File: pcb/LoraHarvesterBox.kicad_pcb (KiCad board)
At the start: 4 copper layers, 48 x 45.5 mm, 42 parts, among them J1 Conn_01x02_Pin, J2 Conn_01x02_Pin, J3 Conn_01x02_Pin, J4 Conn_01x04_Socket, J5 Conn_01x04_Socket, J6 Conn_01x04_Socket, J7 Conn_01x04_Socket, J8 Conn_01x06_Socket, SW1 SSSS811101, SW2 TS-1088-AR02016, U1 BQ25570, U2 RAK3172-8-SM-I, U3 FM24V10-GTR_C466851

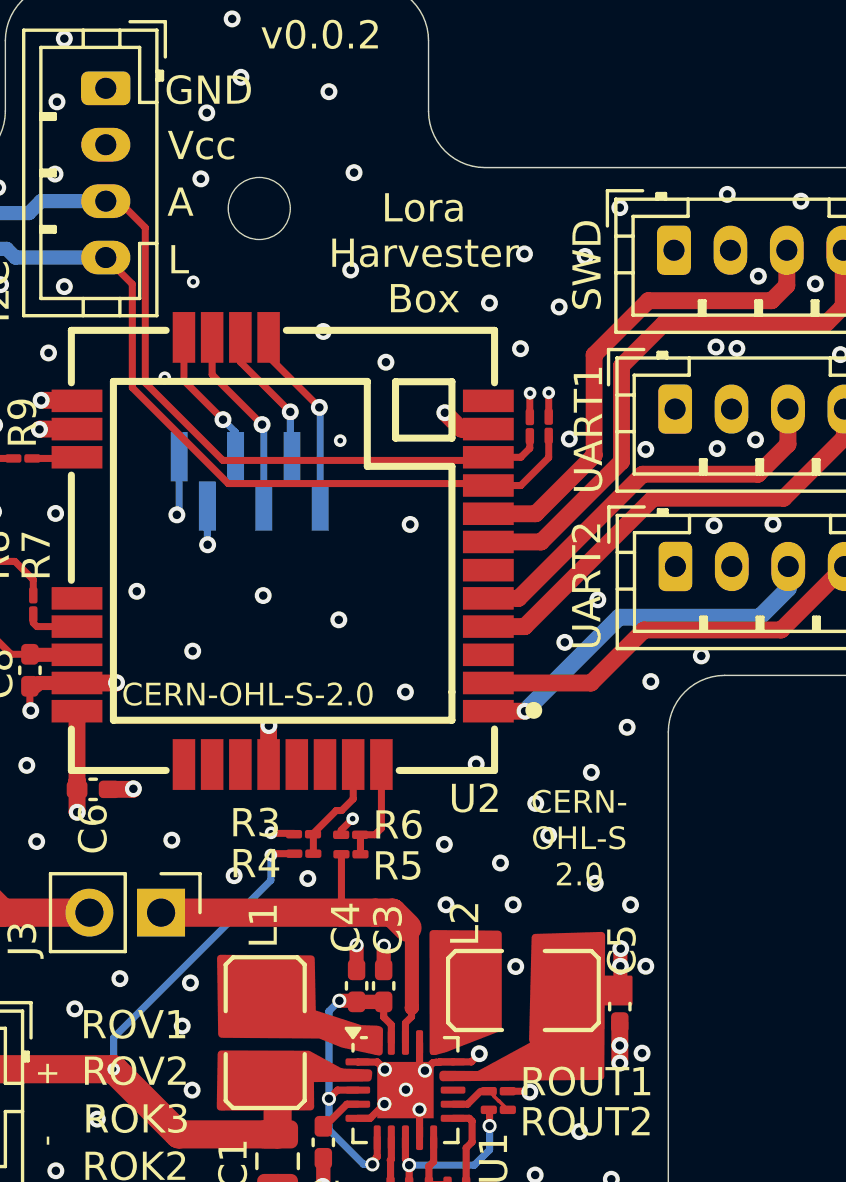
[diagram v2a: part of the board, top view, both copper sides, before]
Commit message: pcb, sch: add resistor values and pretty up the pcb a bit
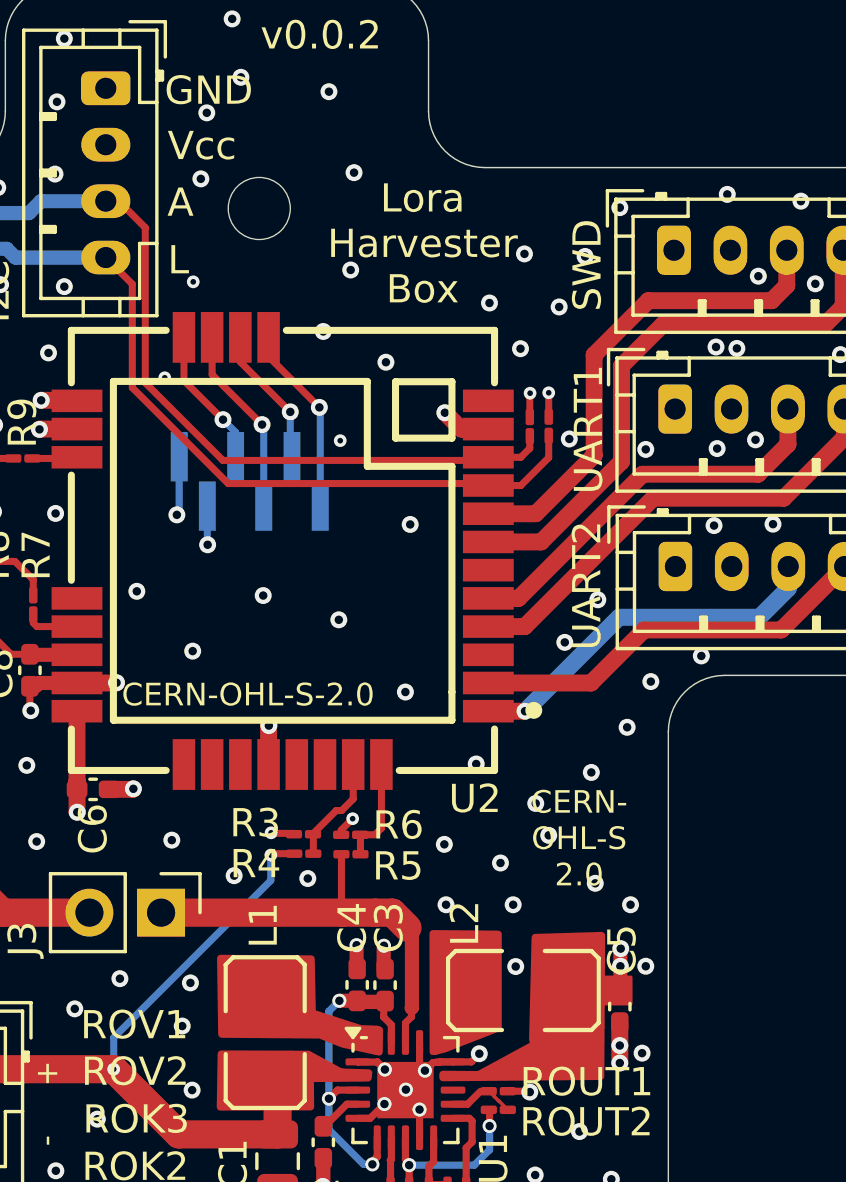
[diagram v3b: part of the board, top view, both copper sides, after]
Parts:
- C1: value C -> 4.7uF
- C2: value C -> 10nF
- C3: renamed from C4; value C -> 0.01uF
- C4: renamed from C3; value CSTOR -> 4.7uF
- ROK1: value R -> 4.3M
- ROK2: value R -> 6.8M
- ROK3: value R -> 1.9M
- ROUT1, ROV2: value R -> 5.1M
- ROUT2: value R -> 7.5M
- ROV1: value R -> 3.9M
- moved C3 1.01 mm to (129.0, 90.0)
- moved C4 0.94 mm to (128.0, 90.0)
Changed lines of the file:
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@@
 			)
 		)
-		(property "Value" "R"
+		(property "Value" "4.3M"
 			(at 0 1 90)
 			(layer "F.Fab")
@@
 	(footprint "Capacitor_SMD:C_0402_1005Metric_Pad0.74x0.62mm_HandSolder"
 		(layer "F.Cu")
-		(at 128.91 90.00625 90)
+		(at 127.97 89.97 90)
 		(descr "Capacitor SMD 0402 (1005 Metric), square (rectangular) end terminal, IPC-7351 nominal with elongated pad for handsoldering. (Body size source: IPC-SM-782 page 76, https://www.pcb-3d.com/wordpress/wp-content/uploads/ipc-sm-782a_amendment_1_and_2.pdf), generated with kicad-footprint-generator")
 		(tags "capacitor handsolder")
-		(property "Reference" "C3"
-			(at 1.98625 0.17 90)
+		(property "Reference" "C4"
+			(at 2.03 -0.16 90)
 			(layer "F.SilkS")
 			(effects
@@
 			)
 		)
-		(property "Value" "CSTOR"
+		(property "Value" "4.7uF"
 			(at 0 1.16 90)
 			(layer "F.Fab")
@@
 			)
 		)
-		(property "Value" "C"
+		(property "Value" "10nF"
 			(at -2.44 5.72 90)
 			(layer "F.Fab")
@@
 			)
 		)
-		(property "Value" "R"
+		(property "Value" "6.8M"
 			(at 0 1 90)
 			(layer "F.Fab")
@@
 			)
 		)
-		(property "Value" "R"
+		(property "Value" "3.9M"
 			(at 0 1 90)
 			(layer "F.Fab")
@@
 	(footprint "Capacitor_SMD:C_0402_1005Metric_Pad0.74x0.62mm_HandSolder"
 		(layer "F.Cu")
-		(at 127.95 90.00375 90)
+		(at 128.96 89.9775 90)
 		(descr "Capacitor SMD 0402 (1005 Metric), square (rectangular) end terminal, IPC-7351 nominal with elongated pad for handsoldering. (Body size source: IPC-SM-782 page 76, https://www.pcb-3d.com/wordpress/wp-content/uploads/ipc-sm-782a_amendment_1_and_2.pdf), generated with kicad-footprint-generator")
 		(tags "capacitor handsolder")
-		(property "Reference" "C4"
-			(at 2.07375 -0.37 90)
+		(property "Reference" "C3"
+			(at 2.0375 0.15 90)
 			(layer "F.SilkS")
 			(effects
@@
 			)
 		)
-		(property "Value" "C"
+		(property "Value" "0.01uF"
 			(at 2.9775 1.51 90)
 			(layer "F.Fab")
@@
 			)
 		)
-		(property "Value" "R"
+		(property "Value" "5.1M"
 			(at 0.2 2.86 0)
 			(layer "F.Fab")
@@
 			)
 		)
-		(property "Value" "C"
+		(property "Value" "4.7uF"
 			(at 0 1.68 270)
 			(layer "F.Fab")
@@
 			)
 		)
-		(property "Value" "R"
+		(property "Value" "1.9M"
 			(at 0.9 5.15 90)
 			(layer "F.Fab")
@@
 			)
 		)
-		(property "Value" "R"
+		(property "Value" "5.1M"
 			(at 0 1 90)
 			(layer "F.Fab")
@@
 			)
 		)
-		(property "Value" "R"
+		(property "Value" "7.5M"
 			(at -9.02 -0.65 0)
 			(layer "F.Fab")
@@
 	)
 	(gr_text "Lora\nHarvester\nBox"
-		(at 130.33 66.25 0)
+		(at 130.29 65.9 0)
 		(layer "F.SilkS")
 		(effects

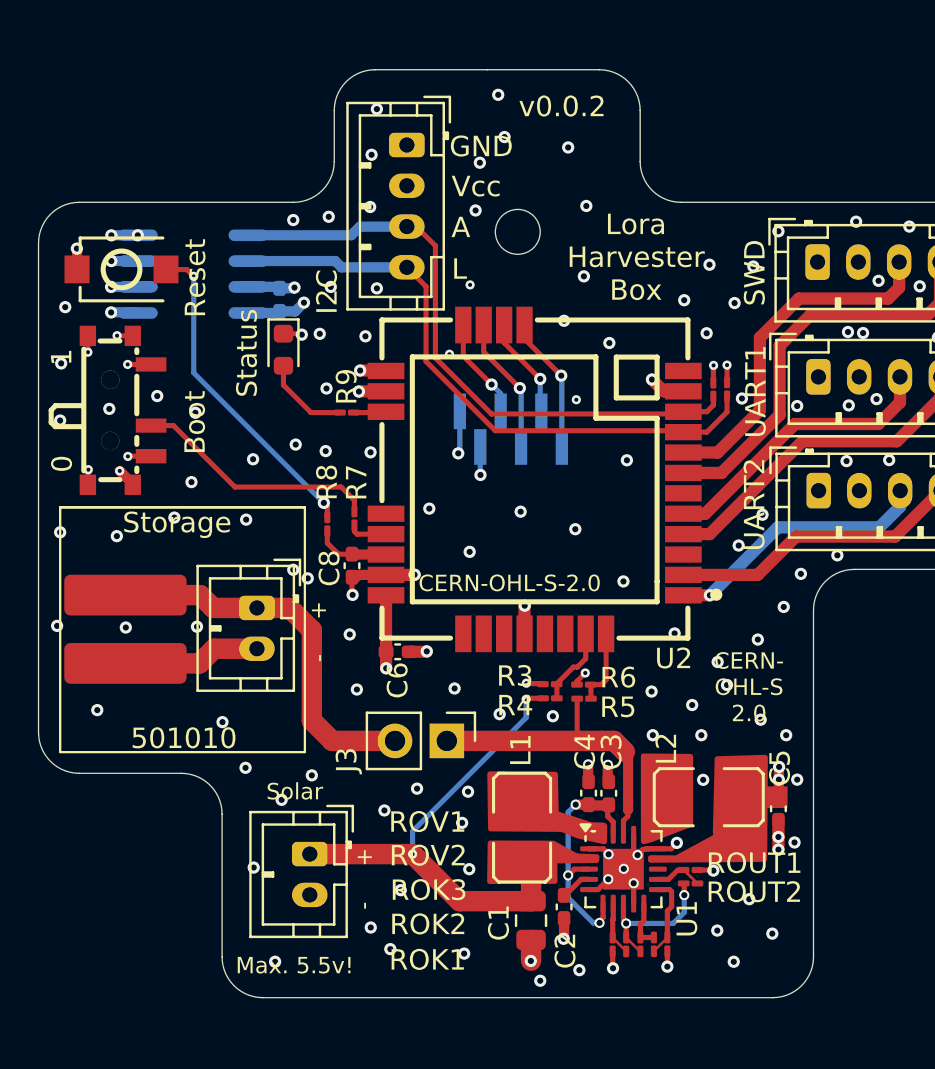
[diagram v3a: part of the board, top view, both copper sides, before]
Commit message: pcb, sch: connect VBAT_OK signal to mirocontroller
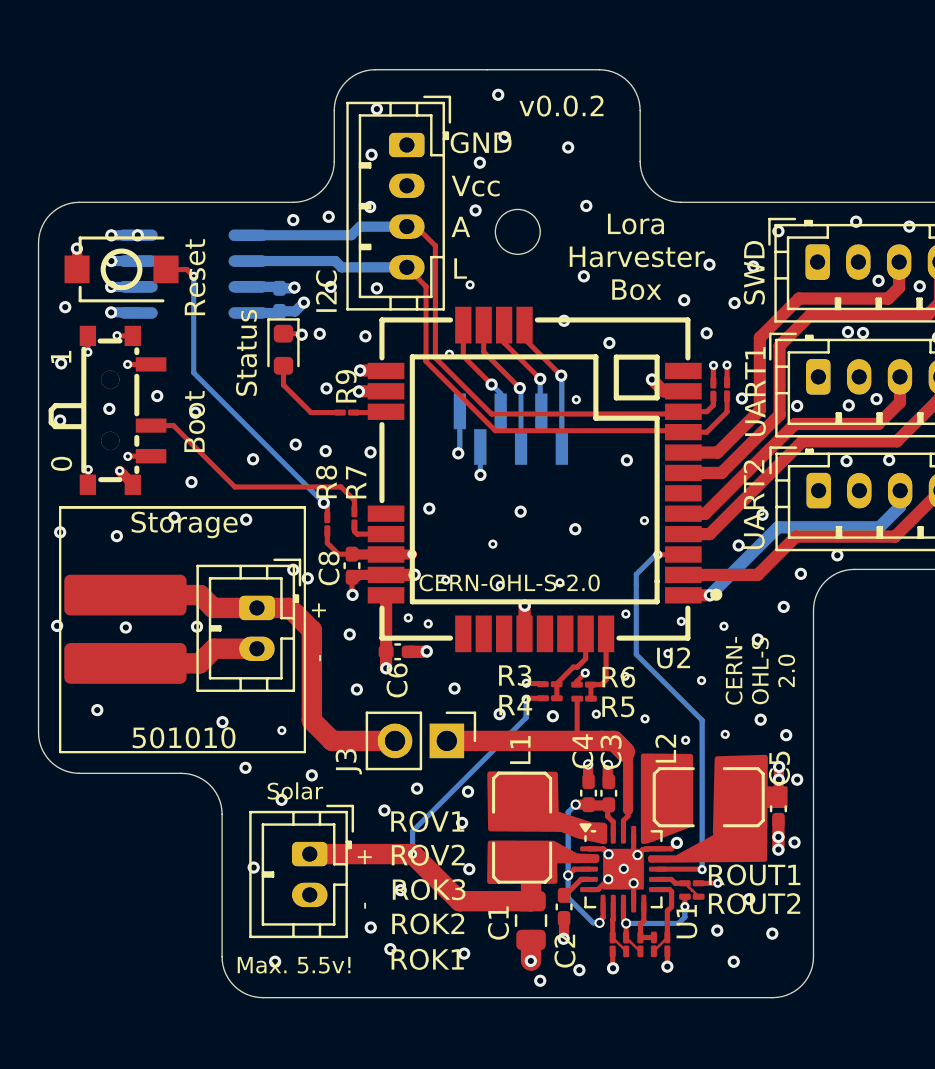
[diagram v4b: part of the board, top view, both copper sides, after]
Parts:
- moved ROUT1 0.65 mm to (133.0, 94.4)
- moved ROUT2 0.65 mm to (133.0, 95.0)
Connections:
- U1 pad 13: unconnected-(U1-VBAT_OK-Pad13) -> /VBAT_OK
- U2 pad 3: unconnected-(U2-PA15/PIN_A4-Pad3) -> /VBAT_OK
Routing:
- net /VBAT_OK: track 0.00 -> 20.7 mm, vias 0 -> 2
- net /RST: track 3.49 -> 4.76 mm, vias 0 -> 1
- net GND: track 51.5 -> 51.6 mm, vias 157 -> 165

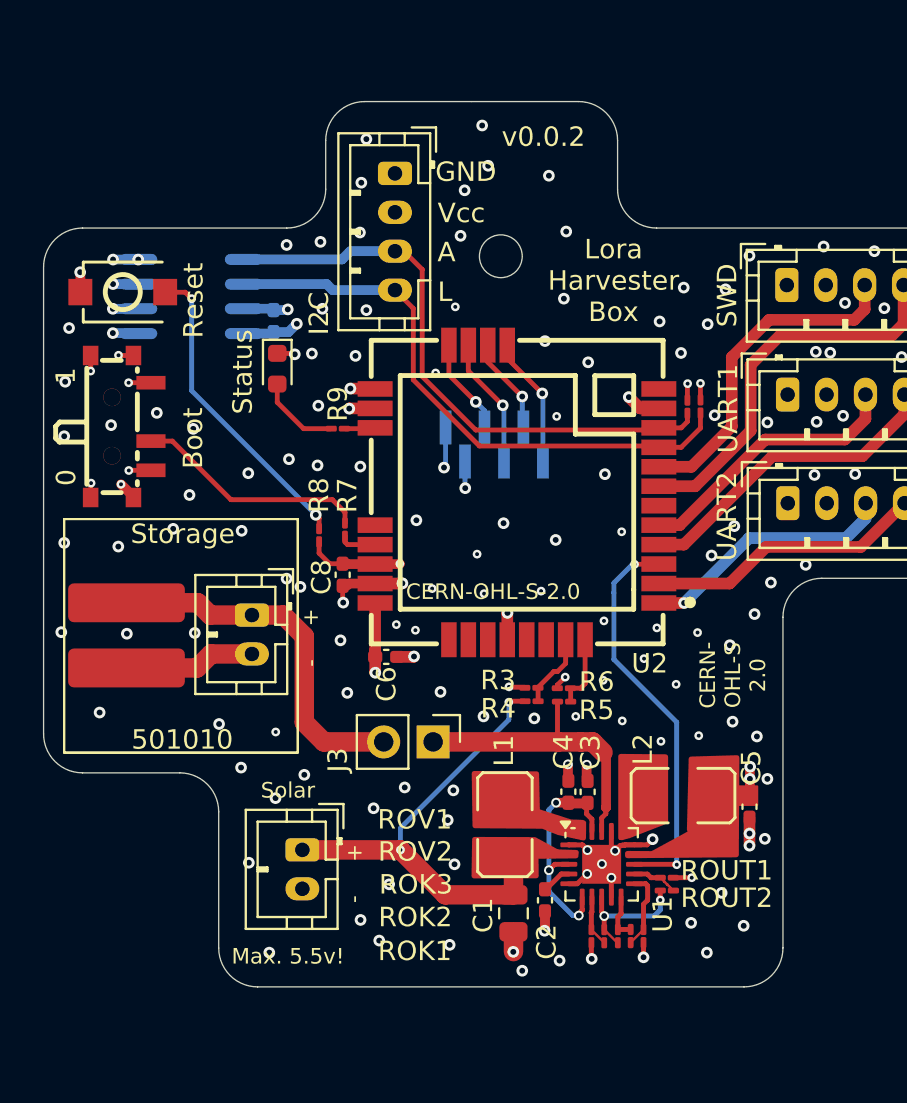
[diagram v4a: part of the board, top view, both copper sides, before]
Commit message: pcb, sch, doc: replace all 402 components with 0603 or 0805.
I cannot solder 0402 in my homelab :-( It starts with the mis-aligned tweezers
and ends with shaking hands.
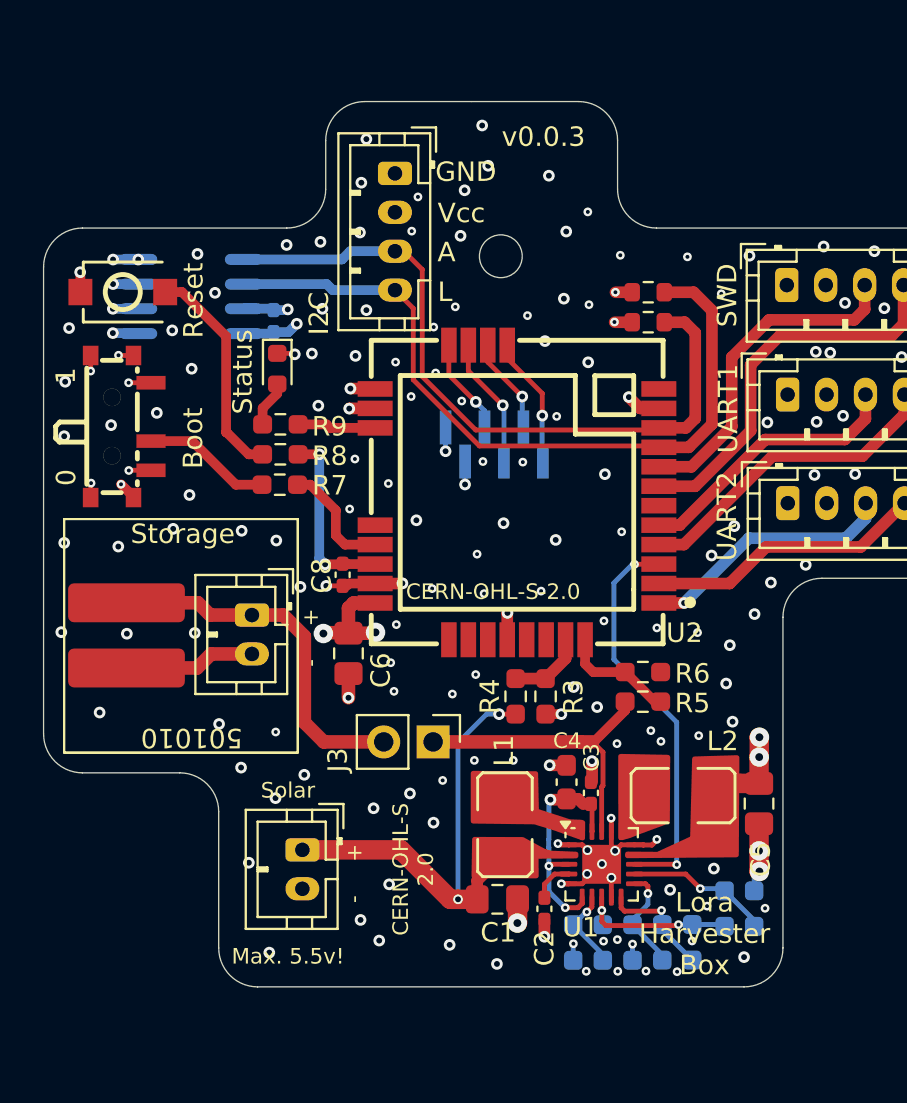
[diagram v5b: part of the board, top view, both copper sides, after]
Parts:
- C1: footprint Capacitor_SMD:C_0805_2012Metric -> Capacitor_SMD:C_0805_2012Metric_Pad1.18x1.45mm_HandSolder
- C4: footprint Capacitor_SMD:C_0402_1005Metric_Pad0.74x0.62mm_HandSolder -> Capacitor_SMD:C_0603_1608Metric_Pad1.08x0.95mm_HandSolder
- C5: value C -> 10uF; footprint Capacitor_SMD:C_0402_1005Metric_Pad0.74x0.62mm_HandSolder -> Capacitor_SMD:C_0805_2012Metric_Pad1.18x1.45mm_HandSolder
- C6: footprint Capacitor_SMD:C_0402_1005Metric_Pad0.74x0.62mm_HandSolder -> Capacitor_SMD:C_0805_2012Metric_Pad1.18x1.45mm_HandSolder
- R1, R2: footprint Resistor_SMD:R_01005_0402Metric_Pad0.57x0.30mm_HandSolder -> Resistor_SMD:R_0603_1608Metric
- R3, R4, R5, R6: value R -> 500k; footprint Resistor_SMD:R_01005_0402Metric_Pad0.57x0.30mm_HandSolder -> Resistor_SMD:R_0603_1608Metric_Pad0.98x0.95mm_HandSolder
- R7, R8, R9: footprint Resistor_SMD:R_01005_0402Metric_Pad0.57x0.30mm_HandSolder -> Resistor_SMD:R_0603_1608Metric_Pad0.98x0.95mm_HandSolder
- ROK1, ROK2, ROK3, ROUT1, ROUT2, ROV1, ROV2: footprint Resistor_SMD:R_01005_0402Metric_Pad0.57x0.30mm_HandSolder -> Resistor_SMD:R_0603_1608Metric_Pad0.98x0.95mm_HandSolder; moved to B.Cu
- moved R2 6.45 mm to (132.1, 64.3), turned to 180 degrees
- moved R1 4.79 mm to (132.1, 65.8), turned to 180 degrees
- moved ROUT1 4.76 mm to (137.5, 96.0), turned to 90 degrees
- moved R8 4.61 mm to (113.2, 72.6), turned to 0 degrees
- moved R6 4.14 mm to (131.8, 83.8), turned to 0 degrees
- moved R7 4.07 mm to (113.1, 74.2), turned to 0 degrees
- moved R5 4.05 mm to (131.8, 85.3)
- moved ROK3 3.84 mm to (134.3, 97.7), turned to -90 degrees
- moved ROUT2 3.11 mm to (136.0, 96.0), turned to 90 degrees
- moved R9 2.96 mm to (113.2, 71.1)
- moved C6 1.95 mm to (116.7, 82.9), turned to 90 degrees
- moved ROK2 1.66 mm to (132.8, 97.7)
- moved C1 1.10 mm to (124.3, 95.5), turned to 0 degrees
- moved ROV1 0.99 mm to (128.2, 97.7)
- moved R4 0.85 mm to (125.3, 85.1), turned to 90 degrees
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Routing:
- net /SCL: track 30.3 -> 38.8 mm
- net /SDA: track 30.6 -> 36.3 mm
- net Net-(R7-Pad1): track 12.0 -> 6.64 mm
- net /RST: track 4.76 -> 9.92 mm, vias 1 -> 2
- net Net-(R8-Pad1): track 16.0 -> 11.4 mm, vias 2 -> 0
- net Net-(U1-VOUT_SET): track 2.34 -> 6.98 mm, vias 0 -> 1
- net /BOOT: track 1.91 -> 6.02 mm
- net +3V0: track 12.2 -> 15.9 mm, vias 8 -> 9
- net Net-(U1-OK_HYST): track 2.39 -> 5.58 mm, vias 0 -> 1
- net Net-(U2-PA8): track 1.54 -> 4.05 mm
- net /ADC_BAT: track 3.79 -> 5.93 mm
- net /VSOLAR: track 24.8 -> 26.8 mm
- net Net-(D1-A): track 4.27 -> 2.38 mm
- net GND: track 51.6 -> 53.3 mm, vias 165 -> 179
- net Net-(U1-VRDIV): track 6.72 -> 8.27 mm
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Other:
- board text added: "CERN-OHL-S 2.0"
- board text added: "v0.0.3"
- board text removed: "501010"
- board text removed: "CERN- OHL-S 2.0"
- board text removed: "v0.0.2"
